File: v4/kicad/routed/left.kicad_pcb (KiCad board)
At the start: 2 copper layers, 160 x 118.6 mm, 68 parts

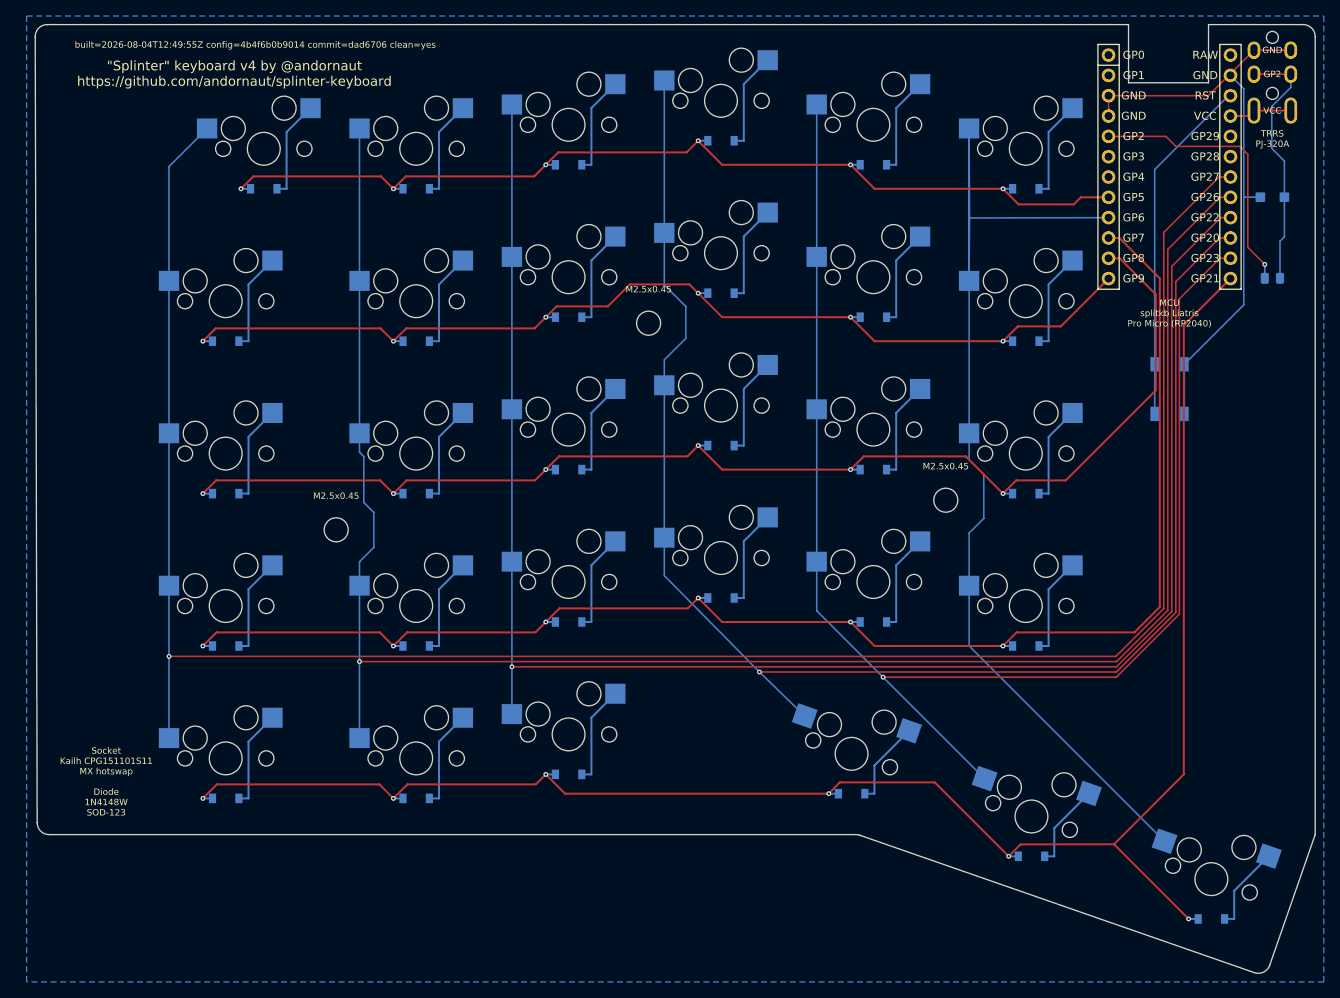
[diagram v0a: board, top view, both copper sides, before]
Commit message: Mirror the halves by construction, and gate that they stay mirrored
The halves' outer board edges were anchored to their own pinky columns, which
differ (left 1.5u; right 1u plus the extra inner column). The left edge picked
up a 0.25mm tilt, so the two outlines were never mirror images and every
clearance measured from that edge differed between the halves. Nothing saw it:
both boards route, pass DRC, fab and assemble.

Both edges now come from one mirrored pair of anchors, edge_outer_top and
edge_outer_bottom, whose base points sit on the right half because that is
where the edge is constrained by a 0.5mm keycap gap. The left half's pinky has
about 10mm of margin and follows the mirror. Only the left bottom corner moves,
0.25mm outward, so every clearance there grows.

validate:symmetry (pipeline step 6) holds the halves to it: the Edge.Cuts
outlines by Hausdorff distance, then every footprint, pad, rule area and silk
text. Pads are matched by name as well as position, since a two-pin part
rotated 180 leaves its pad positions unchanged and swaps which net sits at
each; that is what pins the TVS's compensating rotation in place. Switches,
matrix diodes and the MCU are held to mirrored placement and orientation
instead, because their pin fields are physically not mirror-symmetric. Hand
routing is not compared.

The board halves are regenerated from the new config.
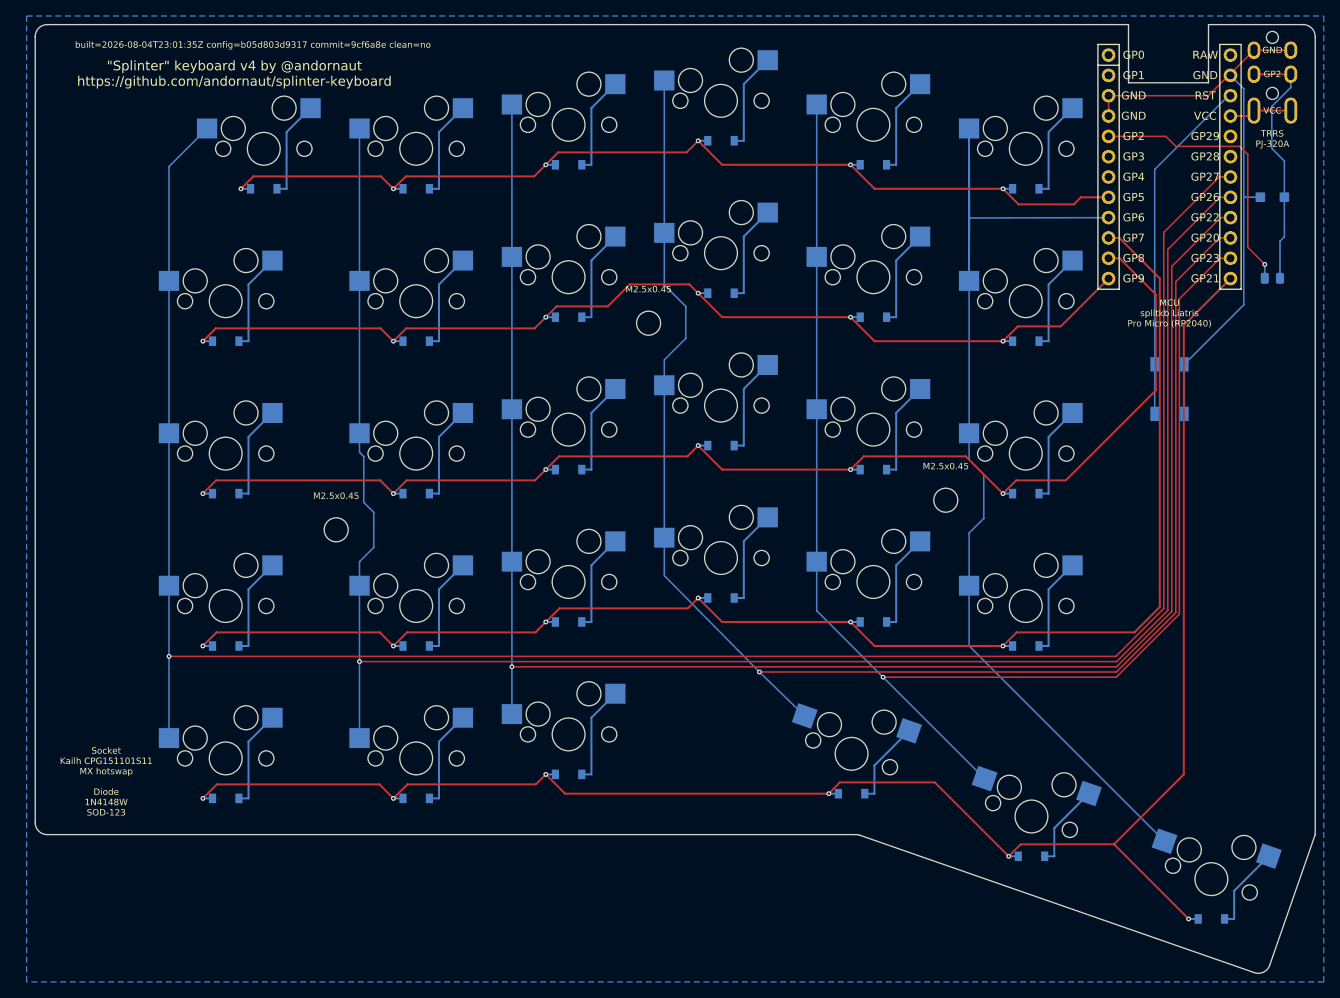
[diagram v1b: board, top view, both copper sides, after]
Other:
- outline, holes or cut-outs redrawn
- board text added: "built=2026-08-04T23:01:35Z config=b05d803d9317 commit=9cf6a8e clean=no"
- board text removed: "built=2026-08-04T12:49:55Z config=4b4f6b0b9014 commit=dad6706 clean=yes"

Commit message: New release version
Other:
- board text added: "built=2026-08-04T23:20:18Z config=b05d803d9317 commit=46645e4 clean=yes"
- board text removed: "built=2026-08-04T23:01:35Z config=b05d803d9317 commit=9cf6a8e clean=no"

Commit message: New release version
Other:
- board text added: "built=2026-08-04T23:55:37Z config=b05d803d9317 commit=96388f1 clean=no"
- board text removed: "built=2026-08-04T23:20:18Z config=b05d803d9317 commit=46645e4 clean=yes"

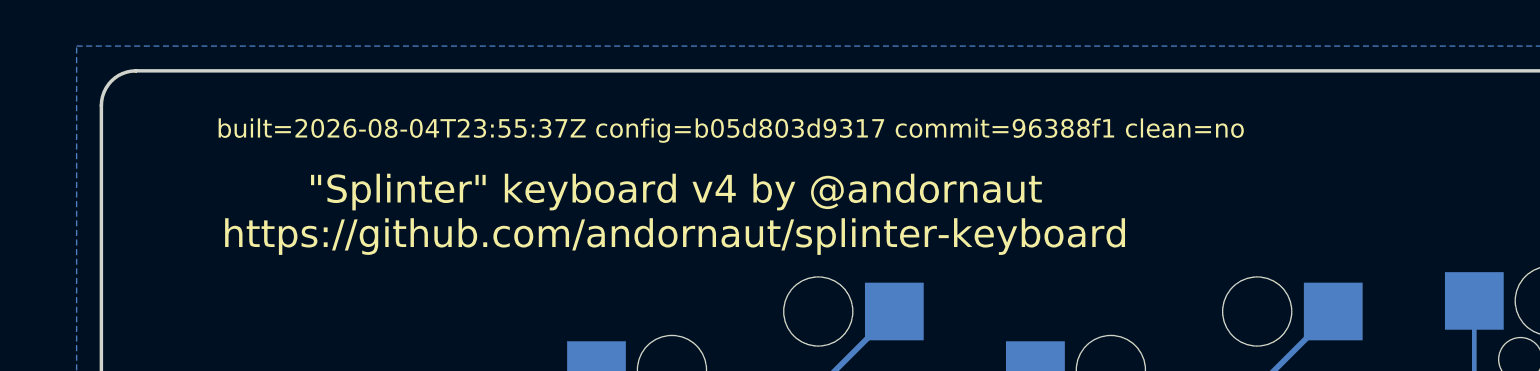
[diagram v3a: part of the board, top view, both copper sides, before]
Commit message: Delete copper buried inside a track of its own net, and say how to rebuild
cleanup-tracks.py keyed duplicates on an exact path, so a segment lying along a
longer one of the same net shared no key with it and outlived every rule here:
both ends sit on the cover's copper, so it is not dangling, and it is not in a
pad. Doubled copper carrying its own net is invisible to DRC, so it reached the
master unremarked. Add a containment rule: same layer, both ends on the other's
centreline, no wider than it, which together mean the copper is already there,
so the delete moves nothing and strands nothing.

Also state each half's dimensions pre- and post-fillet as tables, split the
case-modelling guidance into the rules it was already a list of, and record that
reproducing a build means checking its commit out and re-running the pipeline.
Lifting kicad/routed/ from that commit gives the previous build's masters, since
a stamp can only ever name its own parent.
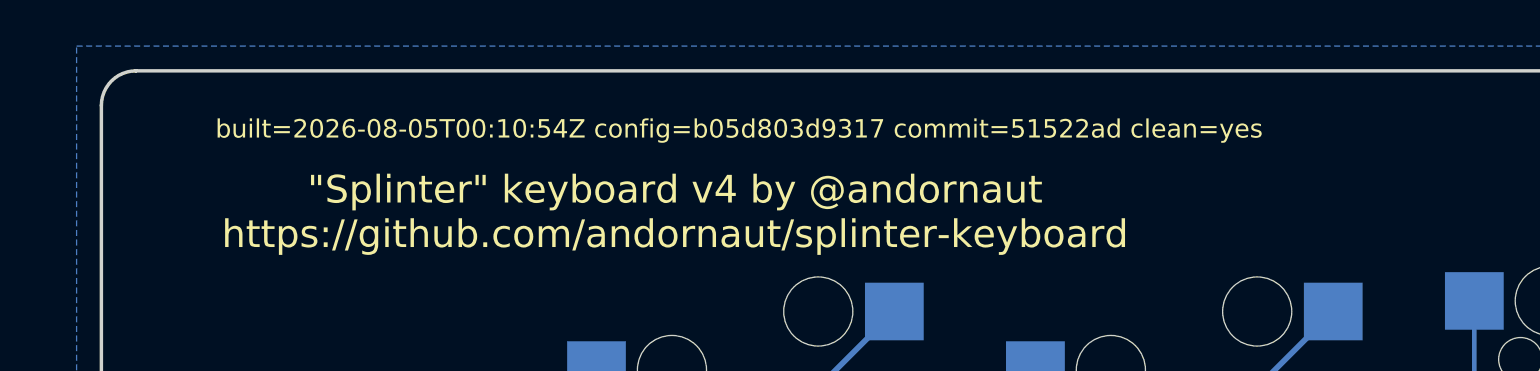
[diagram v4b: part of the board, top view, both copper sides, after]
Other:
- board text added: "built=2026-08-05T00:10:54Z config=b05d803d9317 commit=51522ad clean=yes"
- board text removed: "built=2026-08-04T23:55:37Z config=b05d803d9317 commit=96388f1 clean=no"

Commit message: Rebuild the boards with the buried-copper rule in force
The right master loses the include_traces_vias stub a route had run along, plus
the collinear fragments the delete freed for the merge: 337 segments to 334. The
left half was already clean. Every gate passes.
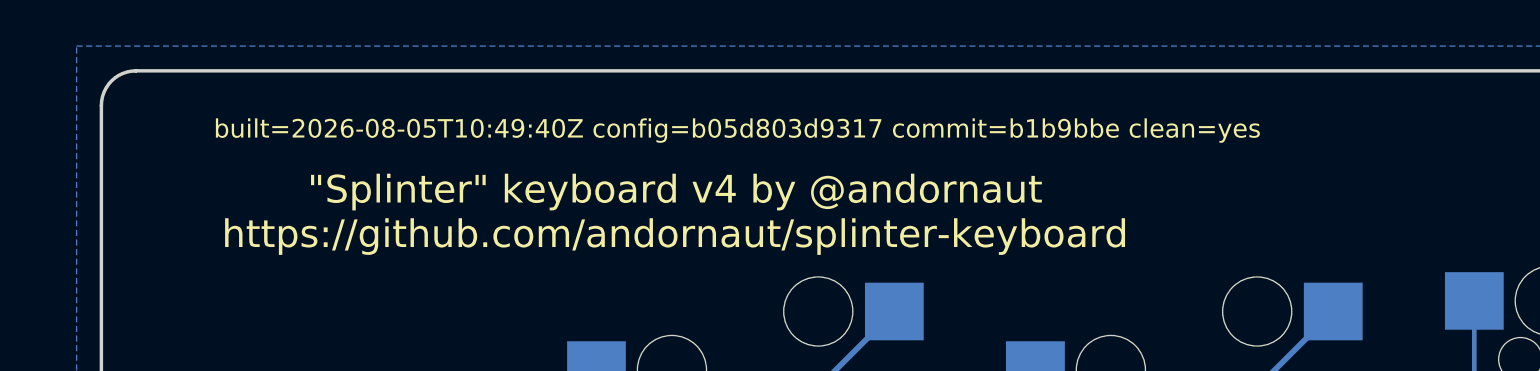
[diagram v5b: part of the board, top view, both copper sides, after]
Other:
- board text added: "built=2026-08-05T10:49:40Z config=b05d803d9317 commit=b1b9bbe clean=yes"
- board text removed: "built=2026-08-05T00:10:54Z config=b05d803d9317 commit=51522ad clean=yes"

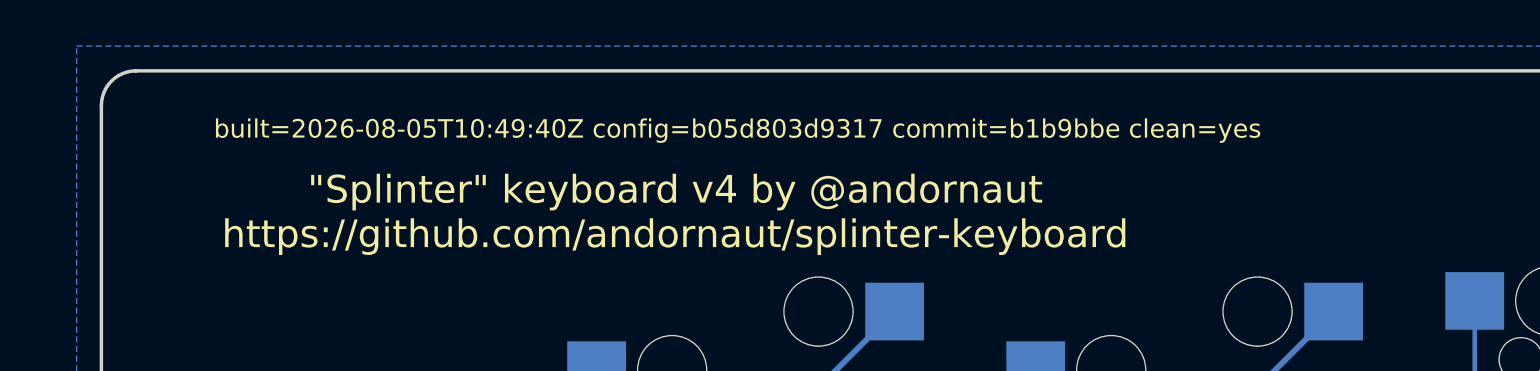
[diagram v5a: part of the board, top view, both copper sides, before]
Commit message: Rebuild the boards on the relocated scripts
Copper, pads, zones and outline are identical to the previous build; the boards
differ only in their provenance stamp and regenerated UUIDs. Every gate passes.
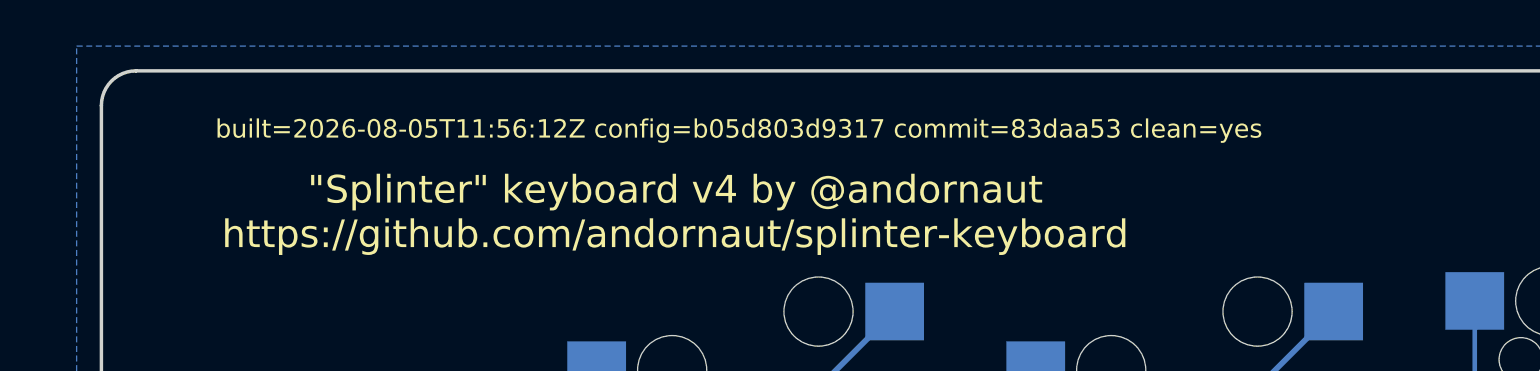
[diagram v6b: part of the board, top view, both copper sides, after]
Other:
- board text added: "built=2026-08-05T11:56:12Z config=b05d803d9317 commit=83daa53 clean=yes"
- board text removed: "built=2026-08-05T10:49:40Z config=b05d803d9317 commit=b1b9bbe clean=yes"

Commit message: Restamp the boards for the new config hash
Adding the un-filleted outlines changed the config.yaml hash, which every board's
stamp carries, so all four are restamped. Copper, pads, zones and outline are
identical to the previous build: no pcbs: entry references those outlines.
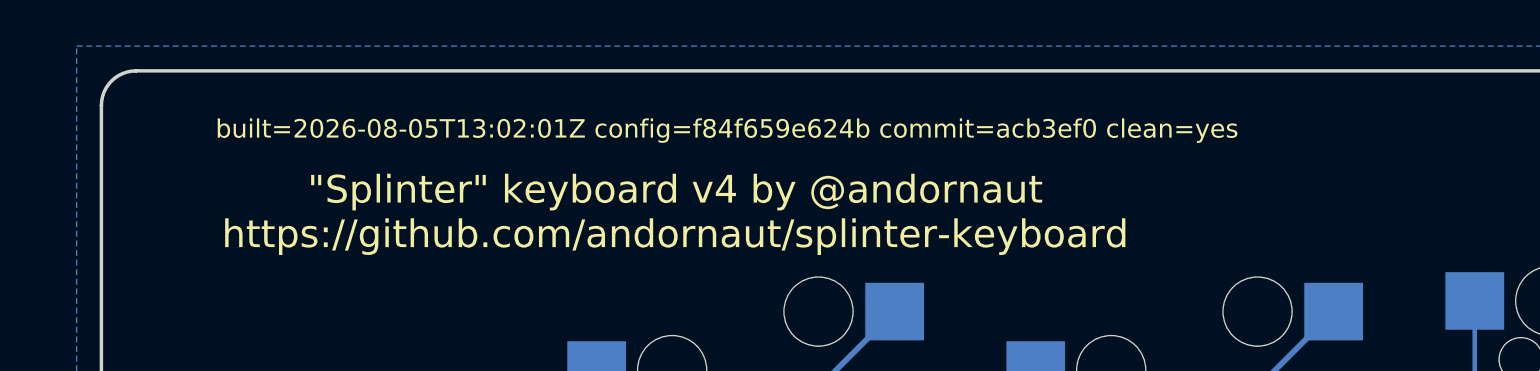
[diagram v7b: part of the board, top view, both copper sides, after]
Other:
- board text added: "built=2026-08-05T13:02:01Z config=f84f659e624b commit=acb3ef0 clean=yes"
- board text removed: "built=2026-08-05T11:56:12Z config=b05d803d9317 commit=83daa53 clean=yes"

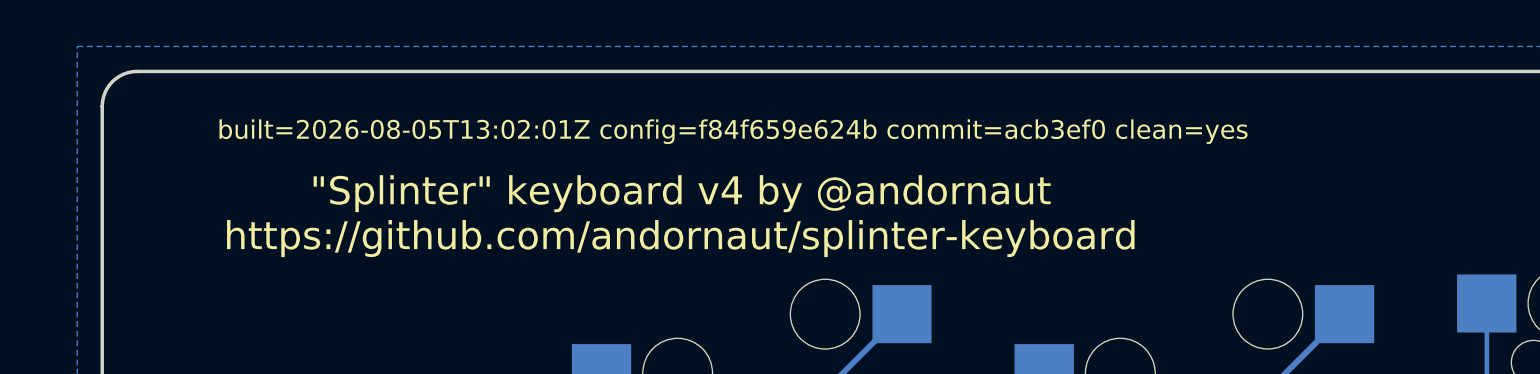
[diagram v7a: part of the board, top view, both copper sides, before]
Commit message: Restamp the boards against the reworked config comment
The stamp keys on the config hash alone, so correcting the comment above
_wallsleft_unfilleted moved every board to stale. Nothing about the design
changed: teardrops hold at 288 left and 303 right, segments at 318 and 334, and
the diff is the stamp plus regenerated UUIDs.

Built from a clean tree so commit= names the source these boards came from.
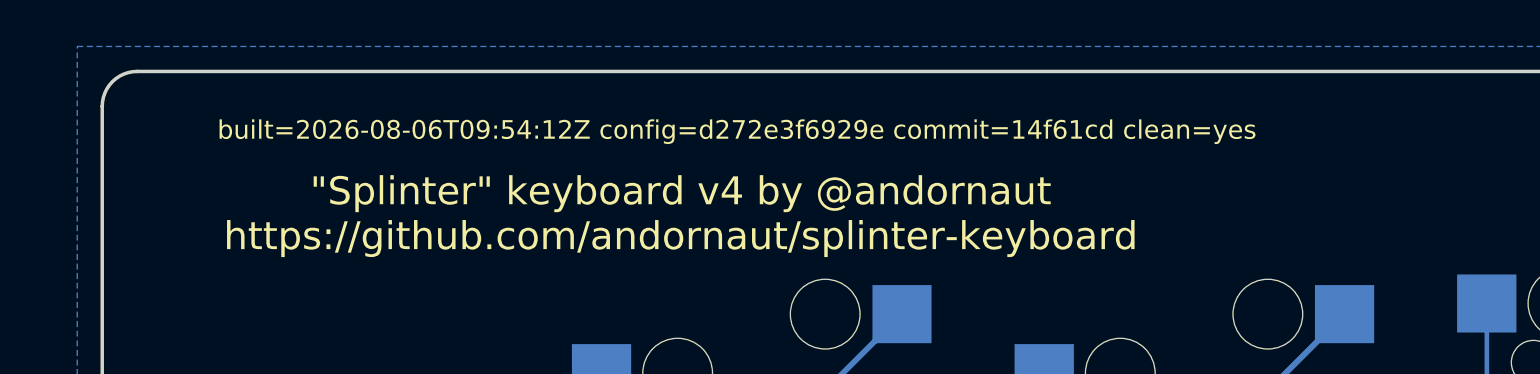
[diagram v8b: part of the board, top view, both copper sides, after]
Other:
- board text added: "built=2026-08-06T09:54:12Z config=d272e3f6929e commit=14f61cd clean=yes"
- board text removed: "built=2026-08-05T13:02:01Z config=f84f659e624b commit=acb3ef0 clean=yes"
